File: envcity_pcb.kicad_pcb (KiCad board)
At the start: 2 copper layers, 42 parts, among them J1 Conn_02x20_Odd_Even, J10 Conn_01x06_Male, J11 Conn_01x06_Male, J12 Conn_01x03_Female, J2 5-1814400-1, J3 Conn_01x02_Male, J4 Conn_01x02_Male, J5 Conn_01x02_Female, J6 Conn_01x06_Male, J7 Conn_01x06_Male, J8 Conn_01x06_Male, J9 Conn_01x06_Male, U1 LM7805_TO220, U2 LM1117-3.3, U3 RFM95W-915S2, U4 ADS1115IDGST, U5 CD74HC4067M, U6 BQ24160RGET, U7 DHT11

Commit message: Add pdf do esquemático. Add arquivo do kicad p/ a PCB.
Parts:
- added D4: 1N47xxA 17V, Diode_THT:D_DO-41_SOD81_P10.16mm_Horizontal, F.Cu at (119.0, 59.0)
- added D5: 1N47xxA 9V, Diode_THT:D_DO-41_SOD81_P10.16mm_Horizontal, F.Cu at (98.0, 59.0)
- added D6: 1N47xxA 5V, Diode_THT:D_DO-41_SOD81_P10.16mm_Horizontal, F.Cu at (104.0, 86.0)
- added Q1: Si2371EDS, Package_TO_SOT_SMD:SOT-23, F.Cu at (126.0, 54.0)
- added Q2: Si2371EDS, Package_TO_SOT_SMD:SOT-23, F.Cu at (105.0, 54.0)
- added Q3: Si2371EDS, Package_TO_SOT_SMD:SOT-23, F.Cu at (99.0, 79.0)
- added R7: 1K, Resistor_SMD:R_0805_2012Metric, F.Cu at (97.0, 43.9)
- added R8: 1K, Resistor_SMD:R_0805_2012Metric, F.Cu at (118.0, 43.9)
- added R9: 1K, Resistor_SMD:R_0805_2012Metric, F.Cu at (89.0, 87.0)
- added U8: BUCK_BOOST_BOARD, 22-23-2061:DIP-4_1889_ELL, F.Cu at (127.0, 19.0)
- J5: value Conn_01x02_Female -> Conn_01x02_Male
- moved C1 171.4 mm to (353.2, 110.1)
- moved U4 171.4 mm to (364.7, 69.2)
- moved C2 171.4 mm to (347.6, 110.1)
- moved C3 171.4 mm to (359.2, 104.2)
- moved C5 171.4 mm to (325.8, 102.9)
- moved D1 171.4 mm to (333.5, 107.8)
- moved D2 171.4 mm to (333.5, 103.5)
- moved J12 171.4 mm to (284.4, 118.7)
- moved U2 171.4 mm to (334.9, 113.8)
- moved U5 171.4 mm to (355.9, 73.9)
- moved C4 171.4 mm to (345.3, 115.7)
- moved C6 171.4 mm to (364.6, 74.3)
- moved U1 171.4 mm to (348.8, 105.3)
- moved R4 112.7 mm to (97.9, 64.0)
- moved U3 112.5 mm to (225.0, 67.0), turned to 270 degrees
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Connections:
- net /BQ24160/Vsistema renamed /Vsys
- C1 pad 1: /Conversores DC-DC/9V_BUCK_BOOST -> /9V_BUCK_BOOST
- C3 pad 1: /Conversores DC-DC/9V_BUCK_BOOST -> /9V_BUCK_BOOST
- D1 pad 1: /Conversores DC-DC/9V_BUCK_BOOST -> /9V_BUCK_BOOST
- D2 pad 1: /Conversores DC-DC/9V_BUCK_BOOST -> /9V_BUCK_BOOST
- J1 pad 1: +3V3 -> /Raspberry PI 4 - Pinout/RASP_3V3
- J1 pad 11: (no net) -> /BQ_INT
- J1 pad 12: (no net) -> /S1
- J1 pad 13: (no net) -> /S0
- J1 pad 16: (no net) -> /S2
- J1 pad 17: +3V3 -> /Raspberry PI 4 - Pinout/RASP_3V3
- J1 pad 18: (no net) -> /S3
- J1 pad 19: (no net) -> /RFM_MOSI
- J1 pad 21: (no net) -> /RFM_MISO
- J1 pad 23: (no net) -> /RFM_SCK
- J1 pad 24: (no net) -> /DIO5
- J1 pad 26: (no net) -> /DHT_OUTPUT
- J1 pad 27: (no net) -> /AD_SDA
- J1 pad 28: (no net) -> /AD_SCL
- J1 pad 29: (no net) -> /DIO1
- J1 pad 3: (no net) -> /BQ_SDA
- J1 pad 31: (no net) -> /DIO4
- J1 pad 32: (no net) -> /AD_ALERT
- J1 pad 33: (no net) -> /DIO2
- J1 pad 35: (no net) -> /NSS
- J1 pad 37: (no net) -> /RESET
- J1 pad 40: (no net) -> /DIO0
- J1 pad 5: (no net) -> /BQ_SCL
- J1 pad 7: (no net) -> /DIO3
- J10 pad 3: (no net) -> /I6
- J10 pad 5: (no net) -> /I7
- J11 pad 3: (no net) -> /I10
- J11 pad 5: (no net) -> /I11
- J12 pad 1: (no net) -> /9V_BUCK_BOOST
- J12 pad 3: (no net) -> /I12
- J3 pad 1: /BQ24160/Vext_dc -> Net-(J3-Pad1)
- J4 pad 1: /BQ24160/VBAT -> Net-(J4-Pad1)
- J5 pad 1: /BQ24160/Vusb -> Net-(J5-Pad1)
- J6 pad 3: (no net) -> /I0
- J6 pad 5: (no net) -> /I1
- J7 pad 3: (no net) -> /I4
- J7 pad 5: (no net) -> /I5
- J8 pad 3: (no net) -> /I8
- J8 pad 5: (no net) -> /I9
- J9 pad 3: (no net) -> /I2
- J9 pad 5: (no net) -> /I3
- R3 pad 2: /BQ24160/BQ_SCL -> /BQ_SCL
- R4 pad 2: /BQ24160/BQ_SDA -> /BQ_SDA
- R5 pad 2: /BQ24160/BQ_INT -> /BQ_INT
- U1 pad 1: /Conversores DC-DC/9V_BUCK_BOOST -> /9V_BUCK_BOOST
- U2 pad 3: /Conversores DC-DC/9V_BUCK_BOOST -> /9V_BUCK_BOOST
- U3 pad 11: (no net) -> /DIO3
- U3 pad 12: (no net) -> /DIO4
- U3 pad 14: (no net) -> /DIO0
- U3 pad 15: (no net) -> /DIO1
- U3 pad 16: (no net) -> /DIO2
- U3 pad 2: (no net) -> /RFM_MISO
- U3 pad 3: (no net) -> /RFM_MOSI
- U3 pad 4: (no net) -> /RFM_SCK
- U3 pad 5: (no net) -> /NSS
- U3 pad 6: (no net) -> /RESET
- U3 pad 7: (no net) -> /DIO5
- U4 pad 10: (no net) -> /AD_SCL
- U4 pad 2: (no net) -> /AD_ALERT
- U4 pad 9: (no net) -> /AD_SDA
- U5 pad 10: (no net) -> /S0
- U5 pad 11: (no net) -> /S1
- U5 pad 13: (no net) -> /S3
- U5 pad 14: (no net) -> /S2
- U5 pad 19: (no net) -> /I12
- U5 pad 2: (no net) -> /I7
- U5 pad 20: (no net) -> /I11
- U5 pad 21: (no net) -> /I10
- U5 pad 22: (no net) -> /I9
- U5 pad 23: (no net) -> /I8
- U5 pad 3: (no net) -> /I6
- U5 pad 4: (no net) -> /I5
- U5 pad 5: (no net) -> /I4
- U5 pad 6: (no net) -> /I3
- U5 pad 7: (no net) -> /I2
- U5 pad 8: (no net) -> /I1
- U5 pad 9: (no net) -> /I0
- U6 pad 3: /BQ24160/BQ_SCL -> /BQ_SCL
- U6 pad 4: /BQ24160/BQ_SDA -> /BQ_SDA
- U6 pad 7: /BQ24160/BQ_INT -> /BQ_INT
- U7 pad 2: (no net) -> /DHT_OUTPUT
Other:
- board outline added: 150 x 100 mm

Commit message: Roteamento da PCB pronto; Agora o 3v3 da raspberry alimenta os resistores de pull up da comunicacao i2c do bq24160
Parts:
- U3: footprint RF_Module:HOPERF_RFM9XW_THT -> RF_Module:HOPERF_RFM9XW_SMD
- moved U1 264.8 mm to (84.0, 100.5), turned to 90 degrees
- moved C3 263.3 mm to (96.0, 112.0)
- moved C1 256.3 mm to (97.0, 103.0), turned to 270 degrees
- moved C2 251.0 mm to (97.0, 96.0), turned to 270 degrees
- moved U2 250.9 mm to (84.0, 118.0), turned to 90 degrees
- moved C4 249.3 mm to (96.0, 119.0)
- moved D2 243.6 mm to (90.0, 110.0), turned to 270 degrees
- moved D1 243.5 mm to (90.0, 104.0), turned to 90 degrees
- moved U4 220.4 mm to (145.0, 87.5)
- moved U5 209.9 mm to (149.5, 112.0)
- moved C6 208.5 mm to (158.0, 102.5)
- moved J12 187.2 mm to (97.5, 131.0), turned to 180 degrees
- moved C5 171.8 mm to (158.0, 66.1), turned to 90 degrees
- moved U8 80.6 mm to (117.0, 99.0), turned to 180 degrees
- moved J7 62.7 mm to (132.0, 131.0), turned to 180 degrees
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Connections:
- J1 pad 1: /Raspberry PI 4 - Pinout/RASP_3V3 -> RASP_3V3
- J1 pad 17: /Raspberry PI 4 - Pinout/RASP_3V3 -> RASP_3V3
- J1 pad 38: (no net) -> /DIO3
- J1 pad 7: /DIO3 -> (no net)
- J2 pad 1: GND -> /Radio LoRa RFM95W/ANT
- J2 pad 2: /Radio LoRa RFM95W/ANT -> GND
- R3 pad 1: +3V3 -> RASP_3V3
- R4 pad 1: +3V3 -> RASP_3V3
- R5 pad 1: +3V3 -> RASP_3V3
- U6 pad 25: (no net) -> GND
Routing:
- net +5V: track 0.00 -> 317.1 mm, vias 0 -> 6
- net +3V3: track 0.00 -> 124.3 mm, vias 0 -> 3
- net /9V_BUCK_BOOST: track 0.00 -> 100.2 mm, vias 0 -> 1
- net /S3: track 0.00 -> 96.0 mm, vias 0 -> 1
- net /S2: track 0.00 -> 92.1 mm, vias 0 -> 2
- net /S1: track 0.00 -> 89.3 mm, vias 0 -> 3
- net /S0: track 0.00 -> 82.6 mm, vias 0 -> 3
- net /AD_ALERT: track 0.00 -> 77.9 mm, vias 0 -> 1
- net /I12: track 0.00 -> 77.7 mm, vias 0 -> 4
- net /DIO5: track 0.00 -> 65.2 mm, vias 0 -> 4
- net GND: track 0.00 -> 64.8 mm
- net /RFM_SCK: track 0.00 -> 60.6 mm, vias 0 -> 2
- net /BQ_INT: track 0.00 -> 55.5 mm, vias 0 -> 2
- net /RFM_MOSI: track 0.00 -> 52.9 mm, vias 0 -> 2
- net /AD_SDA: track 0.00 -> 51.8 mm
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- added copper zone on B.Cu, net GND
- added copper zone on F.Cu, net GND
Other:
- board size 150 x 100 mm -> 100 x 100 mm

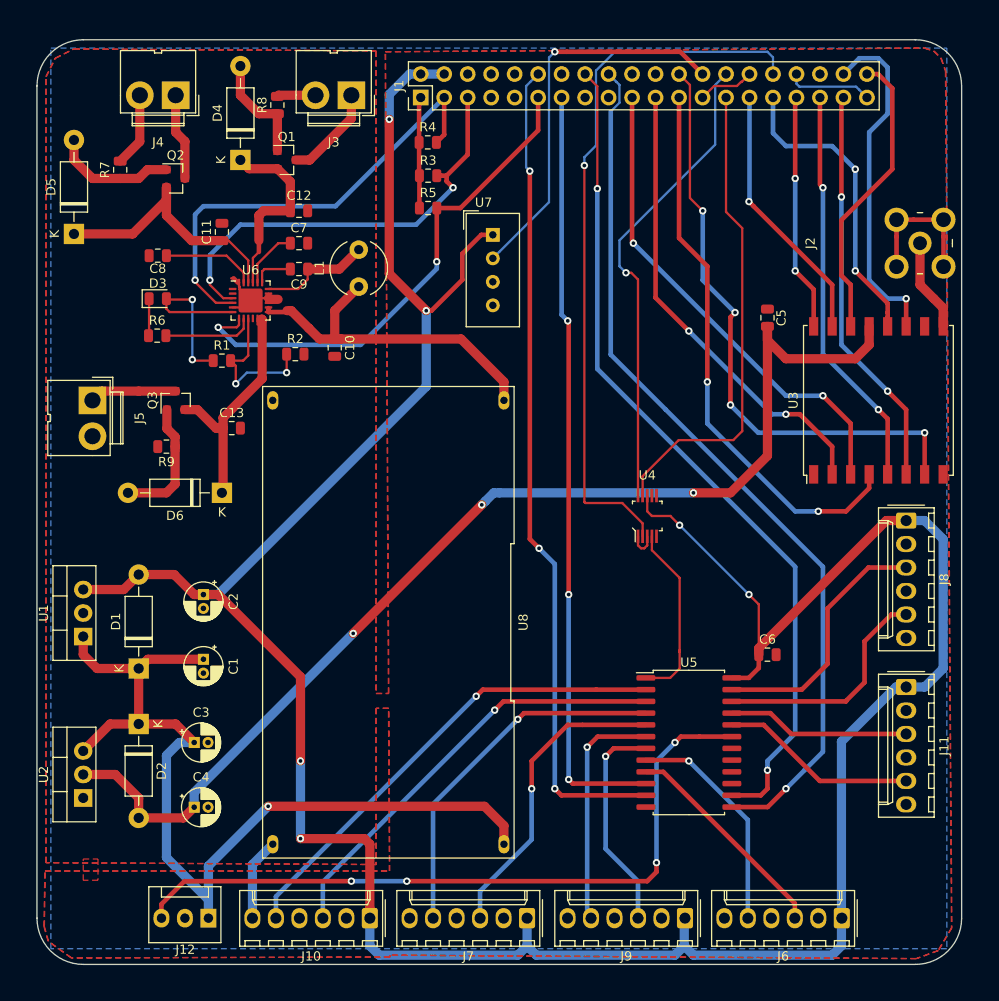
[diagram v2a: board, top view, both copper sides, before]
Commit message: Add mounting holes. Corrige footprint dos conectores da bateria e alimentacao
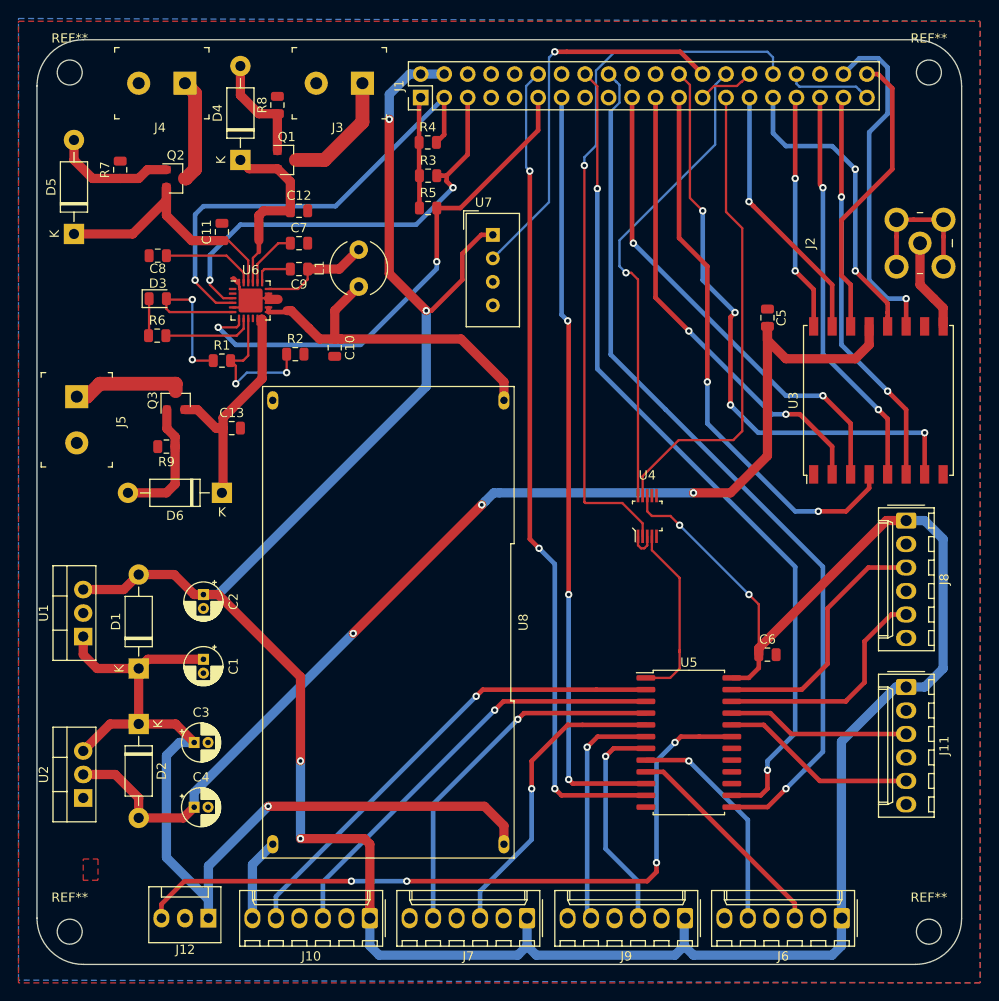
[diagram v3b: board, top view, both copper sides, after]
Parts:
- added REF**: MountingHole_2.7mm, MountingHole:MountingHole_2.7mm, F.Cu at (175.5, 132.5)
- added REF**: MountingHole_2.7mm, MountingHole:MountingHole_2.7mm, F.Cu at (175.5, 39.5)
- added REF**: MountingHole_2.7mm, MountingHole:MountingHole_2.7mm, F.Cu at (82.5, 39.5)
- added REF**: MountingHole_2.7mm, MountingHole:MountingHole_2.7mm, F.Cu at (82.5, 132.5)
- J3, J4, J5: footprint Connector:JWT_A3963_1x02_P3.96mm_Vertical -> digikey-footprints:Term_Block_1x2_P5mm
- moved J3 1.77 mm to (114.2, 40.7)
- moved J5 1.75 mm to (83.3, 74.6)
- moved J4 1.64 mm to (95.0, 40.7)
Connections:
- U6 pad 25: GND -> (no net)
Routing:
- net GND: track 64.8 -> 52.7 mm
- net Net-(J5-Pad1): track 9.41 -> 12.8 mm
- net Net-(J3-Pad1): track 10.4 -> 13.1 mm
- net Net-(J4-Pad1): track 9.41 -> 11.3 mm

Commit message: vish
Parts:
- U6: footprint Package_DFN_QFN:QFN-24-1EP_4x4mm_P0.5mm_EP2.6x2.6mm -> Package_DFN_QFN:QFN-24-1EP_4x4mm_P0.5mm_EP2.6x2.6mm_ThermalVias
- moved C11 7.04 mm to (92.1, 55.4), turned to 180 degrees
- moved R2 5.48 mm to (112.0, 72.0)
- moved C10 3.71 mm to (107.7, 68.1)
- moved L1 2.53 mm to (112.8, 65.0)
- moved C13 2.26 mm to (99.0, 80.0), turned to 180 degrees
- moved R1 1.84 mm to (97.2, 70.7)
- moved Q2 0.99 mm to (93.5, 50.1), turned to 90 degrees
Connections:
- U6 pad 25: (no net) -> GND
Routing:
- net /Vsys: track 37.8 -> 0.00 mm
- net /BQ24160/Vusb: track 29.2 -> 0.00 mm
- net /BQ24160/VBAT: track 26.3 -> 5.05 mm
- net /BQ24160/Vext_dc: track 20.7 -> 0.00 mm
- net Net-(D5-Pad2): track 13.4 -> 0.00 mm
- net Net-(J4-Pad1): track 11.3 -> 0.00 mm
- net /BQ24160/PMIDU: track 10.2 -> 0.00 mm
- net /BQ24160/BAT_NTC: track 16.9 -> 23.9 mm
- net Net-(C7-Pad1): track 6.49 -> 0.00 mm
- net /BQ24160/VDRV: track 20.0 -> 17.7 mm, vias 2 -> 1
- net /BQ24160/SW: track 12.2 -> 10.3 mm
- net Net-(J5-Pad1): track 12.8 -> 10.9 mm
- net GND: track 52.7 -> 52.9 mm, vias 0 -> 86
- added copper zone on F.Cu, net /BQ24160/PMIDU
- added copper zone on F.Cu, net /BQ24160/VBAT
- added copper zone on F.Cu, net /BQ24160/Vext_dc
- added copper zone on F.Cu, net /BQ24160/Vusb
- added copper zone on F.Cu, net /Vsys
- added copper zone on F.Cu, net Net-(C7-Pad1)
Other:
- board text added: "Mateus M. Roncaglio Marcio S. Oyamada Edson T. Camargo Universidade Estadual do Oeste do Paraná - UNIOESTE Universidade Tecnológica Federal do Paraná - UTFPR"
- board text added: "REV2.0"

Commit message: v3
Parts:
- removed C1, C3: 0,33uF, Capacitor_THT:CP_Radial_D4.0mm_P1.50mm
- removed C10, C11, C12, C13, C6: 1uF, Capacitor_SMD:C_0805_2012Metric
- removed C2, C4: 0,1uF, Capacitor_THT:CP_Radial_D4.0mm_P1.50mm
- removed C5: 100nF, Capacitor_SMD:C_0805_2012Metric
- removed C7, C8: 4,7uF, Capacitor_SMD:C_0805_2012Metric
- removed C9: 0,01uF, Capacitor_SMD:C_0805_2012Metric
- removed D1, D2: 1N4001, Diode_THT:D_DO-41_SOD81_P10.16mm_Horizontal
- removed D3: LED, LED_SMD:LED_0805_2012Metric
- removed D4: 1N47xxA 17V, Diode_THT:D_DO-41_SOD81_P10.16mm_Horizontal
- removed D5: 1N47xxA 9V, Diode_THT:D_DO-41_SOD81_P10.16mm_Horizontal
- removed D6: 1N47xxA 5V, Diode_THT:D_DO-41_SOD81_P10.16mm_Horizontal
- removed J1: Conn_02x20_Odd_Even, Connector_PinHeader_2.54mm:PinHeader_2x20_P2.54mm_Vertical
- removed J10, J11, J6, J7, J8, J9: Conn_01x06_Male, Connector_Molex:Molex_KK-254_AE-6410-06A_1x06_P2.54mm_Vertical
- removed J12: Conn_01x03_Female, Connector:FanPinHeader_1x03_P2.54mm_Vertical
- removed J2: 5-1814400-1, digikey-footprints:RF_SMA_RightAngle_5-1814400-1
- removed J3, J4, J5: Conn_01x02_Male, digikey-footprints:Term_Block_1x2_P5mm
- removed L1: 1,5uH, Inductor_THT:L_Radial_D6.0mm_P4.00mm
- removed Q1, Q2, Q3: Si2371EDS, Package_TO_SOT_SMD:SOT-23
- removed R1, R3, R4, R5: 10k, Resistor_SMD:R_0805_2012Metric
- removed R2: 10K, Resistor_SMD:R_0805_2012Metric
- removed R6, R7, R8, R9: 1K, Resistor_SMD:R_0805_2012Metric
- removed REF** (x4): MountingHole_2.7mm, MountingHole:MountingHole_2.7mm
- removed U1: LM7805_TO220, Package_TO_SOT_THT:TO-220-3_Vertical
- removed U2: LM1117-3.3, Package_TO_SOT_THT:TO-220-3_Vertical
- removed U3: RFM95W-915S2, RF_Module:HOPERF_RFM9XW_SMD
- removed U4: ADS1115IDGST, digikey-footprints:MSOP-10_W3mm
- removed U5: CD74HC4067M, Package_SO:SOIC-24W_7.5x15.4mm_P1.27mm
- removed U6: BQ24160RGET, Package_DFN_QFN:QFN-24-1EP_4x4mm_P0.5mm_EP2.6x2.6mm_ThermalVias
- removed U7: DHT11, Sensor:Aosong_DHT11_5.5x12.0_P2.54mm
- removed U8: BUCK_BOOST_BOARD, 22-23-2061:DIP-4_1889_ELL
- added MK1: M2.5, MountingHole:MountingHole_2.7mm_M2.5, F.Cu at (203.5, 97.5)
- added MK2: M2.5, MountingHole:MountingHole_2.7mm_M2.5, F.Cu at (261.5, 97.5)
- added MK3: M2.5, MountingHole:MountingHole_2.7mm_M2.5, F.Cu at (203.5, 146.5)
- added MK4: M2.5, MountingHole:MountingHole_2.7mm_M2.5, F.Cu at (261.5, 146.5)
- added P1: Conn_02x20_Odd_Even, Connector_PinSocket_2.54mm:PinSocket_2x20_P2.54mm_Vertical, B.Cu at (208.4, 98.8)
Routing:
- net +5V: track 317.1 -> 0.00 mm, vias 6 -> 0
- net +3V3: track 124.3 -> 0.00 mm, vias 3 -> 0
- net /9V_BUCK_BOOST: track 100.2 -> 0.00 mm, vias 1 -> 0
- net /S3: track 96.0 -> 0.00 mm, vias 1 -> 0
- net /S2: track 92.1 -> 0.00 mm, vias 2 -> 0
- net /S1: track 89.3 -> 0.00 mm, vias 3 -> 0
- net /S0: track 82.6 -> 0.00 mm, vias 3 -> 0
- net /AD_ALERT: track 77.9 -> 0.00 mm, vias 1 -> 0
- net /I12: track 77.7 -> 0.00 mm, vias 4 -> 0
- net /DIO5: track 65.2 -> 0.00 mm, vias 4 -> 0
- net /RFM_SCK: track 60.6 -> 0.00 mm, vias 2 -> 0
- net /BQ_INT: track 55.5 -> 0.00 mm, vias 2 -> 0
- net GND: track 52.9 -> 0.00 mm, vias 86 -> 0
- net /RFM_MOSI: track 52.9 -> 0.00 mm, vias 2 -> 0
- net /AD_SDA: track 51.8 -> 0.00 mm
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- removed copper zone on F.Cu, net /BQ24160/PMIDU
- removed copper zone on F.Cu, net /BQ24160/VBAT
- removed copper zone on F.Cu, net /BQ24160/Vext_dc
- removed copper zone on F.Cu, net /BQ24160/Vusb
- removed copper zone on F.Cu, net /Vsys
- removed copper zone on B.Cu, net GND
- removed copper zone on F.Cu, net GND
- removed copper zone on F.Cu, net Net-(C7-Pad1)
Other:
- board size 100 x 100 mm -> 65 x 56 mm
- net class Default: trace_width 0.25 -> 0.2; via_dia 0.8 -> 0.9; via_drill 0.4 -> 0.6
- net class Power added: clearance 0.2, trace_width 0.5, via_dia 1, via_drill 0.7
- rule pad_to_mask_clearance: 0.051 -> 0
- rule trace_min: 0.2 -> 0.1524
- rule via_min_drill: 0.3 -> 0.5
- rule via_min_size: 0.4 -> 0.8
- board text added: "DISPLAY"
- board text added: "RASPBERRY-PI 40-PIN ADDON BOARD VIEW FROM TOP NOTE: P1 SHOULD BE FITTED ON THE REVERSE OF THE BOARD ADD EDGE CUTS FROM CAMERA AND DISPLAY PORTS AS REQUIRED"
- board text added: "RJ45"
- board text added: "USB"
- board text removed: "Mateus M. Roncaglio Marcio S. Oyamada Edson T. Camargo Universidade Estadual do Oeste do Paraná - UNIOESTE Universidade Tecnológica Federal do Paraná - UTFPR"
- board text removed: "REV2.0"
